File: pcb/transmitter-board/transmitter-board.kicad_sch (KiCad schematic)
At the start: 0 parts

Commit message: Add transmitter-board schematics
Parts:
- added BT1: Battery, Battery:BatteryHolder_Keystone_1042_1x18650, symbol Device:Battery
- added C1: 1n, Capacitor_SMD:C_0805_2012Metric_Pad1.18x1.45mm_HandSolder, symbol Device:C
- added C2: 10n, Capacitor_SMD:C_0805_2012Metric_Pad1.18x1.45mm_HandSolder, symbol Device:C
- added C4, C6: 0.1u, Capacitor_SMD:C_0805_2012Metric_Pad1.18x1.45mm_HandSolder, symbol Device:C
- added C7: 10u, Capacitor_SMD:C_0805_2012Metric_Pad1.18x1.45mm_HandSolder, symbol Device:C
- added D1: R LED, LED_SMD:LED_0805_2012Metric_Pad1.15x1.40mm_HandSolder, symbol Device:LED
- added D2: B LED, LED_SMD:LED_0805_2012Metric_Pad1.15x1.40mm_HandSolder, symbol Device:LED
- added D5: IR LED, LED_THT:LED_D1.8mm_W1.8mm_H2.4mm_Horizontal_O3.81mm_Z8.2mm, symbol Device:LED
- added J1: USB_C_Receptacle_PowerOnly_6P, Connector_USB:USB_C_Receptacle_GCT_USB4125-xx-x-0190_6P_TopMnt_Horizontal, symbol Connector:USB_C_Receptacle_PowerOnly_6P
- added Q1: BC817, Package_TO_SOT_SMD:SOT-23, symbol Transistor_BJT:BC817
- added Q3, Q4: AO3400A, Package_TO_SOT_SMD:SOT-23, symbol Transistor_FET:AO3400A
- added R1, R4, R7, R9: 1k, Resistor_SMD:R_0805_2012Metric_Pad1.20x1.40mm_HandSolder, symbol Device:R
- added R10: 100R, Resistor_SMD:R_0805_2012Metric_Pad1.20x1.40mm_HandSolder, symbol Device:R
- added R11: 18, Resistor_SMD:R_0805_2012Metric_Pad1.20x1.40mm_HandSolder, symbol Device:R
- added R12: 180, Resistor_SMD:R_0805_2012Metric_Pad1.20x1.40mm_HandSolder, symbol Device:R
- added R2: 18.4k, Resistor_SMD:R_0805_2012Metric_Pad1.20x1.40mm_HandSolder, symbol Device:R
- added R3, R6: 5.1k, Resistor_SMD:R_0805_2012Metric_Pad1.20x1.40mm_HandSolder, symbol Device:R
- added R5: 1.2k, Resistor_SMD:R_0805_2012Metric_Pad1.20x1.40mm_HandSolder, symbol Device:R
- added U1: NE555D, Package_SO:SOIC-8_3.9x4.9mm_P1.27mm, symbol Timer:NE555D
- added U3: TP4056-42-ESOP8, Package_SO:SOIC-8-1EP_3.9x4.9mm_P1.27mm_EP2.41x3.3mm_ThermalVias, symbol Battery_Management:TP4056-42-ESOP8
- added U4: DW01A, Package_TO_SOT_SMD:SOT-23-6, symbol Battery_Management:DW01A
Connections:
- new net: R7.1, U3.7 (~{CHRG})
- new net: D1.1 (K), R7.2
- new net: R9.1, U4.2 (CS)
- new net: Q4.1 (G), U4.1 (OD)
- new net: Q3.1 (G), U4.3 (OC)
- new net: C6.1, R10.2, U4.5 (VCC)
- new net: Q3.3 (D), Q4.3 (D)
- new net: R5.1, U3.2 (PROG)
- new net: R4.1, U3.6 (~{STDBY})
- new net: D2.1 (K), R4.2
- new net: C1.1, R2.2, U1.2 (TR), U1.6 (THR)
- new net: R1.2, R2.1, U1.7 (DIS)
- new net: C2.1, U1.5 (CV)
- new net: J1.B5 (CC2), R3.1
- new net: J1.A5 (CC1), R6.1
- new net: D5.1 (K), Q1.3 (C)
- new net: D5.2 (A), R11.2
- new net: Q1.1 (B), R12.2
- new net +3V8: BT1.1 (+), C7.1, R1.1, R10.1, R11.1, U1.4 (R), U1.8 (VCC), U3.5 (BAT)
- new net 555OUT: R12.1, U1.3 (Q)
- new net GND: BT1.2 (-), C1.2, C2.2, C4.2, C6.2, C7.2, J1.A12 (GND), J1.B12 (GND), Q1.2 (E), Q3.2 (S), Q4.2 (S), R3.2, R5.2, R6.2, R9.2, U1.1 (GND), U3.1 (TEMP), U3.3 (GND), U4.6 (GND)
- new net IN+: C4.1, D1.2 (A), D2.2 (A), J1.A9 (VBUS), J1.B9 (VBUS), U3.4 (V_{CC}), U3.8 (CE)
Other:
- note added: "Battery Charger"
- note added: "Battery Protection"
- note added: "IR Diode Circuit"
- note added: "Square Wave Generator (38.175 kHz, 51.32% duty cycle)"
- note added: "USB Connector"

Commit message: Change package to 0603
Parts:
- C1, C2, C4, C6, C7: footprint Capacitor_SMD:C_0805_2012Metric_Pad1.18x1.45mm_HandSolder -> Capacitor_SMD:C_0603_1608Metric_Pad1.08x0.95mm_HandSolder
- D1, D2: footprint LED_SMD:LED_0805_2012Metric_Pad1.15x1.40mm_HandSolder -> LED_SMD:LED_0603_1608Metric_Pad1.05x0.95mm_HandSolder
- R1, R10, R11, R12, R2, R3, R4, R5, R6, R7, R9: footprint Resistor_SMD:R_0805_2012Metric_Pad1.20x1.40mm_HandSolder -> Resistor_SMD:R_0603_1608Metric_Pad0.98x0.95mm_HandSolder
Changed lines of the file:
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@@
 			)
 		)
-		(property "Footprint" "Capacitor_SMD:C_0805_2012Metric_Pad1.18x1.45mm_HandSolder"
+		(property "Footprint" "Capacitor_SMD:C_0603_1608Metric_Pad1.08x0.95mm_HandSolder"
 			(at 65.7352 129.54 0)
 			(effects
@@
 			)
 		)
-		(property "Footprint" "Resistor_SMD:R_0805_2012Metric_Pad1.20x1.40mm_HandSolder"
+		(property "Footprint" "Resistor_SMD:R_0603_1608Metric_Pad0.98x0.95mm_HandSolder"
 			(at 57.912 106.68 90)
 			(effects
@@
 			)
 		)
-		(property "Footprint" "Resistor_SMD:R_0805_2012Metric_Pad1.20x1.40mm_HandSolder"
+		(property "Footprint" "Resistor_SMD:R_0603_1608Metric_Pad0.98x0.95mm_HandSolder"
 			(at 79.502 102.87 90)
 			(effects
@@
 			)
 		)
-		(property "Footprint" "Capacitor_SMD:C_0805_2012Metric_Pad1.18x1.45mm_HandSolder"
+		(property "Footprint" "Capacitor_SMD:C_0603_1608Metric_Pad1.08x0.95mm_HandSolder"
 			(at 122.2248 99.06 0)
 			(effects
@@
 			)
 		)
-		(property "Footprint" "Resistor_SMD:R_0805_2012Metric_Pad1.20x1.40mm_HandSolder"
+		(property "Footprint" "Resistor_SMD:R_0603_1608Metric_Pad0.98x0.95mm_HandSolder"
 			(at 27.178 102.87 90)
 			(effects
@@
 			)
 		)
-		(property "Footprint" "Resistor_SMD:R_0805_2012Metric_Pad1.20x1.40mm_HandSolder"
+		(property "Footprint" "Resistor_SMD:R_0603_1608Metric_Pad0.98x0.95mm_HandSolder"
 			(at 61.722 106.68 90)
 			(effects
@@
 			)
 		)
-		(property "Footprint" "Capacitor_SMD:C_0805_2012Metric_Pad1.18x1.45mm_HandSolder"
+		(property "Footprint" "Capacitor_SMD:C_0603_1608Metric_Pad1.08x0.95mm_HandSolder"
 			(at 69.5452 60.96 0)
 			(effects
@@
 			)
 		)
-		(property "Footprint" "Resistor_SMD:R_0805_2012Metric_Pad1.20x1.40mm_HandSolder"
+		(property "Footprint" "Resistor_SMD:R_0603_1608Metric_Pad0.98x0.95mm_HandSolder"
 			(at 74.422 48.26 90)
 			(effects
@@
 			)
 		)
-		(property "Footprint" "Capacitor_SMD:C_0805_2012Metric_Pad1.18x1.45mm_HandSolder"
+		(property "Footprint" "Capacitor_SMD:C_0603_1608Metric_Pad1.08x0.95mm_HandSolder"
 			(at 36.5252 62.23 0)
 			(effects
@@
 			)
 		)
-		(property "Footprint" "Resistor_SMD:R_0805_2012Metric_Pad1.20x1.40mm_HandSolder"
+		(property "Footprint" "Resistor_SMD:R_0603_1608Metric_Pad0.98x0.95mm_HandSolder"
 			(at 70.612 175.26 90)
 			(effects
@@
 			)
 		)
-		(property "Footprint" "LED_SMD:LED_0805_2012Metric_Pad1.15x1.40mm_HandSolder"
+		(property "Footprint" "LED_SMD:LED_0603_1608Metric_Pad1.05x0.95mm_HandSolder"
 			(at 59.69 115.57 0)
 			(effects
@@
 			)
 		)
-		(property "Footprint" "LED_SMD:LED_0805_2012Metric_Pad1.15x1.40mm_HandSolder"
+		(property "Footprint" "LED_SMD:LED_0603_1608Metric_Pad1.05x0.95mm_HandSolder"
 			(at 63.5 115.57 0)
 			(effects
@@
 			)
 		)
-		(property "Footprint" "Resistor_SMD:R_0805_2012Metric_Pad1.20x1.40mm_HandSolder"
+		(property "Footprint" "Resistor_SMD:R_0603_1608Metric_Pad0.98x0.95mm_HandSolder"
 			(at 118.11 89.408 90)
 			(effects
@@
 			)
 		)
-		(property "Footprint" "Capacitor_SMD:C_0805_2012Metric_Pad1.18x1.45mm_HandSolder"
+		(property "Footprint" "Capacitor_SMD:C_0603_1608Metric_Pad1.08x0.95mm_HandSolder"
 			(at 110.7948 95.25 0)
 			(effects
@@
 			)
 		)
-		(property "Footprint" "Resistor_SMD:R_0805_2012Metric_Pad1.20x1.40mm_HandSolder"
+		(property "Footprint" "Resistor_SMD:R_0603_1608Metric_Pad0.98x0.95mm_HandSolder"
 			(at 129.032 27.94 90)
 			(effects
@@
 			)
 		)
-		(property "Footprint" "Resistor_SMD:R_0805_2012Metric_Pad1.20x1.40mm_HandSolder"
+		(property "Footprint" "Resistor_SMD:R_0603_1608Metric_Pad0.98x0.95mm_HandSolder"
 			(at 79.502 175.26 90)
 			(effects
@@
 			)
 		)
-		(property "Footprint" "Resistor_SMD:R_0805_2012Metric_Pad1.20x1.40mm_HandSolder"
+		(property "Footprint" "Resistor_SMD:R_0603_1608Metric_Pad0.98x0.95mm_HandSolder"
 			(at 74.422 38.1 90)
 			(effects
@@
 			)
 		)
-		(property "Footprint" "Resistor_SMD:R_0805_2012Metric_Pad1.20x1.40mm_HandSolder"
+		(property "Footprint" "Resistor_SMD:R_0603_1608Metric_Pad0.98x0.95mm_HandSolder"
 			(at 115.57 51.308 90)
 			(effects

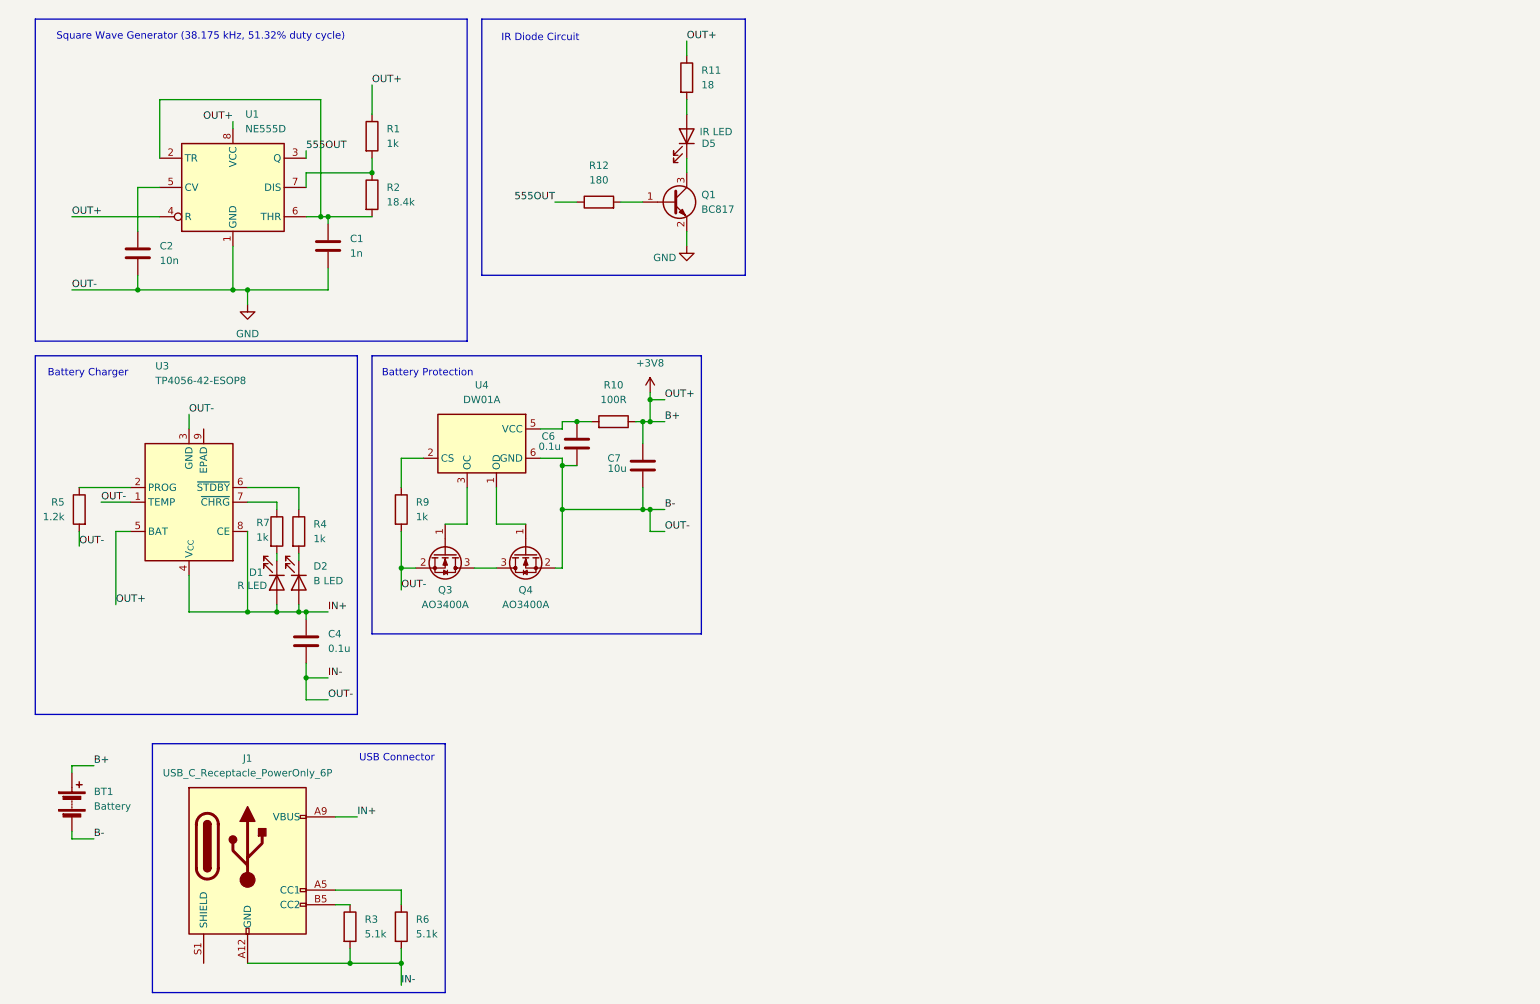
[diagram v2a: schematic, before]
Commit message: Add transmitter-board pcb
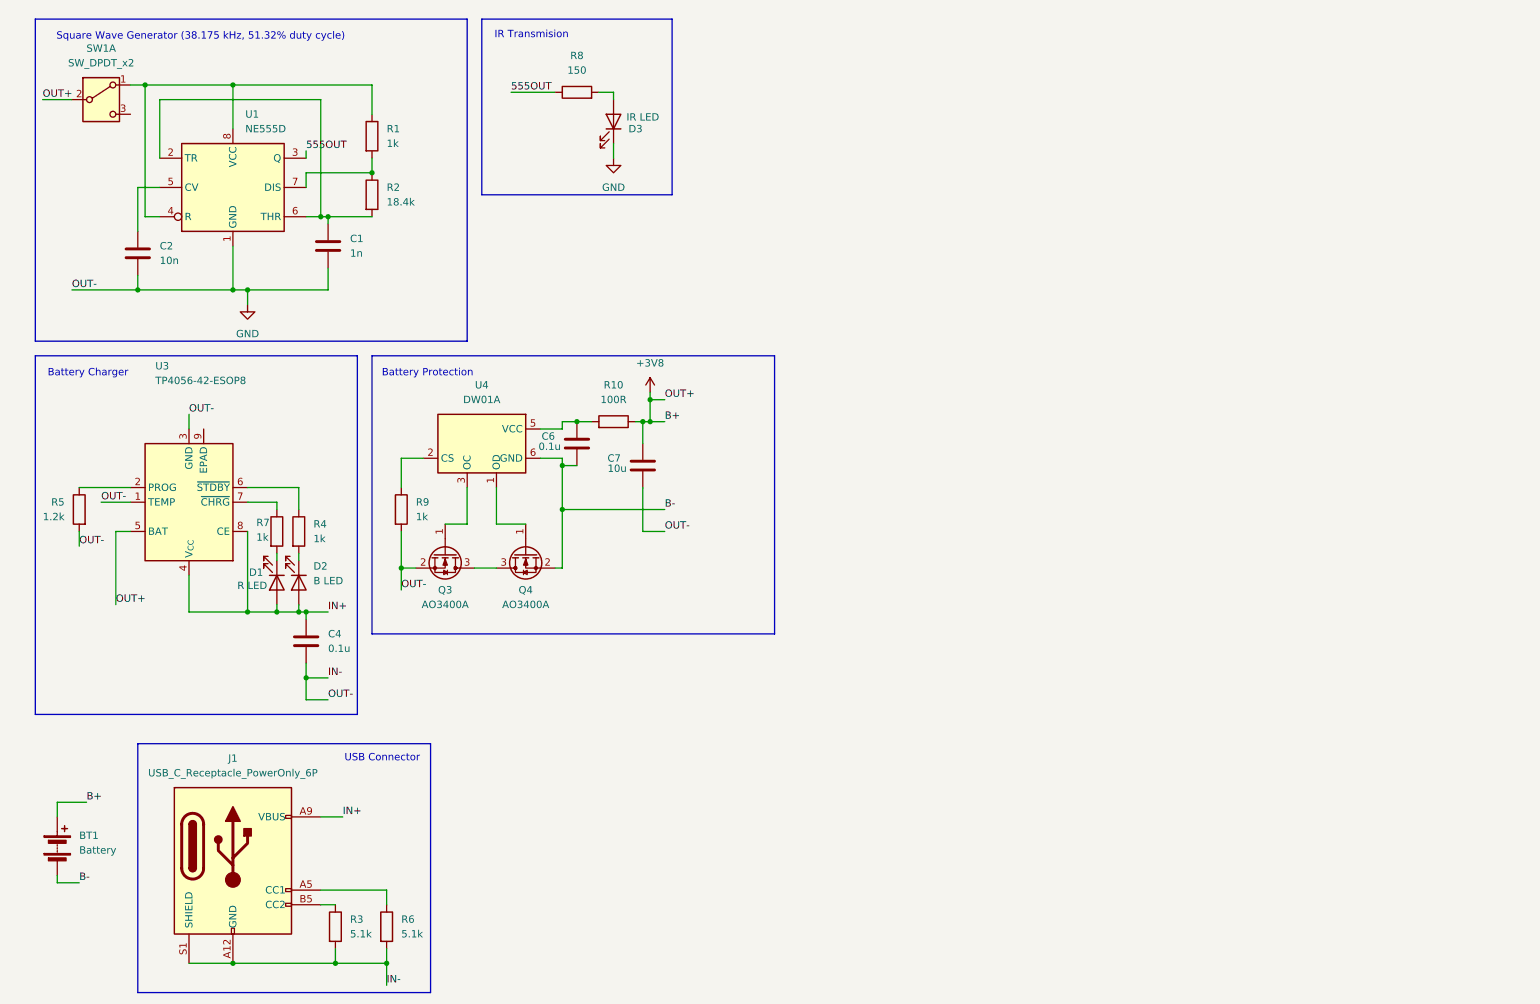
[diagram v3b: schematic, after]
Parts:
- removed D5: IR LED, LED_THT:LED_D1.8mm_W1.8mm_H2.4mm_Horizontal_O3.81mm_Z8.2mm, symbol Device:LED
- removed Q1: BC817, Package_TO_SOT_SMD:SOT-23, symbol Transistor_BJT:BC817
- removed R11: 18, Resistor_SMD:R_0603_1608Metric_Pad0.98x0.95mm_HandSolder, symbol Device:R
- removed R12: 180, Resistor_SMD:R_0603_1608Metric_Pad0.98x0.95mm_HandSolder, symbol Device:R
- added D3: IR LED, LED_THT:LED_THT_Horizontal_SMD_mounted, symbol Device:LED
- added R8: 150, Resistor_SMD:R_0603_1608Metric_Pad0.98x0.95mm_HandSolder, symbol Device:R
- added SW1: SW_DPDT_x2, Button_Switch_SMD:SW_DPDT_CK_JS202011JCQN, symbol Switch:SW_DPDT_x2
- BT1: footprint Battery:BatteryHolder_Keystone_1042_1x18650 -> Connector_PinSocket_2.54mm:PinSocket_1x02_P2.54mm_Vertical_SMD_Pin1Left
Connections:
- net +3V8: now also SW1.2 (B); no longer R1.1, U1.4 (R), U1.8 (VCC)
- net 555OUT: now also R8.1
- net GND: now also J1.S1 (SHIELD), D3.1 (K); no longer BT1.2 (-), C6.2, Q4.2 (S), U4.6 (GND)
- new net: R1.1, SW1.1 (A), U1.4 (R), U1.8 (VCC)
- new net: D3.2 (A), R8.2
- new net B-: BT1.2 (-), C6.2, Q4.2 (S), U4.6 (GND)
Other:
- note added: "IR Transmision"
- note removed: "IR Diode Circuit"
- moved on the sheet: BT1, J1, R3, R6

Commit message: Change hole size under TP4056 and change battery connector to THT.
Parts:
- BT1: footprint Connector_PinSocket_2.54mm:PinSocket_1x02_P2.54mm_Vertical_SMD_Pin1Left -> Connector_PinSocket_2.54mm:PinSocket_1x02_P2.54mm_Vertical
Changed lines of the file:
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@@
 			)
 		)
-		(property "Footprint" "Connector_PinSocket_2.54mm:PinSocket_1x02_P2.54mm_Vertical_SMD_Pin1Left"
+		(property "Footprint" "Connector_PinSocket_2.54mm:PinSocket_1x02_P2.54mm_Vertical"
 			(at 21.59 159.766 90)
 			(effects

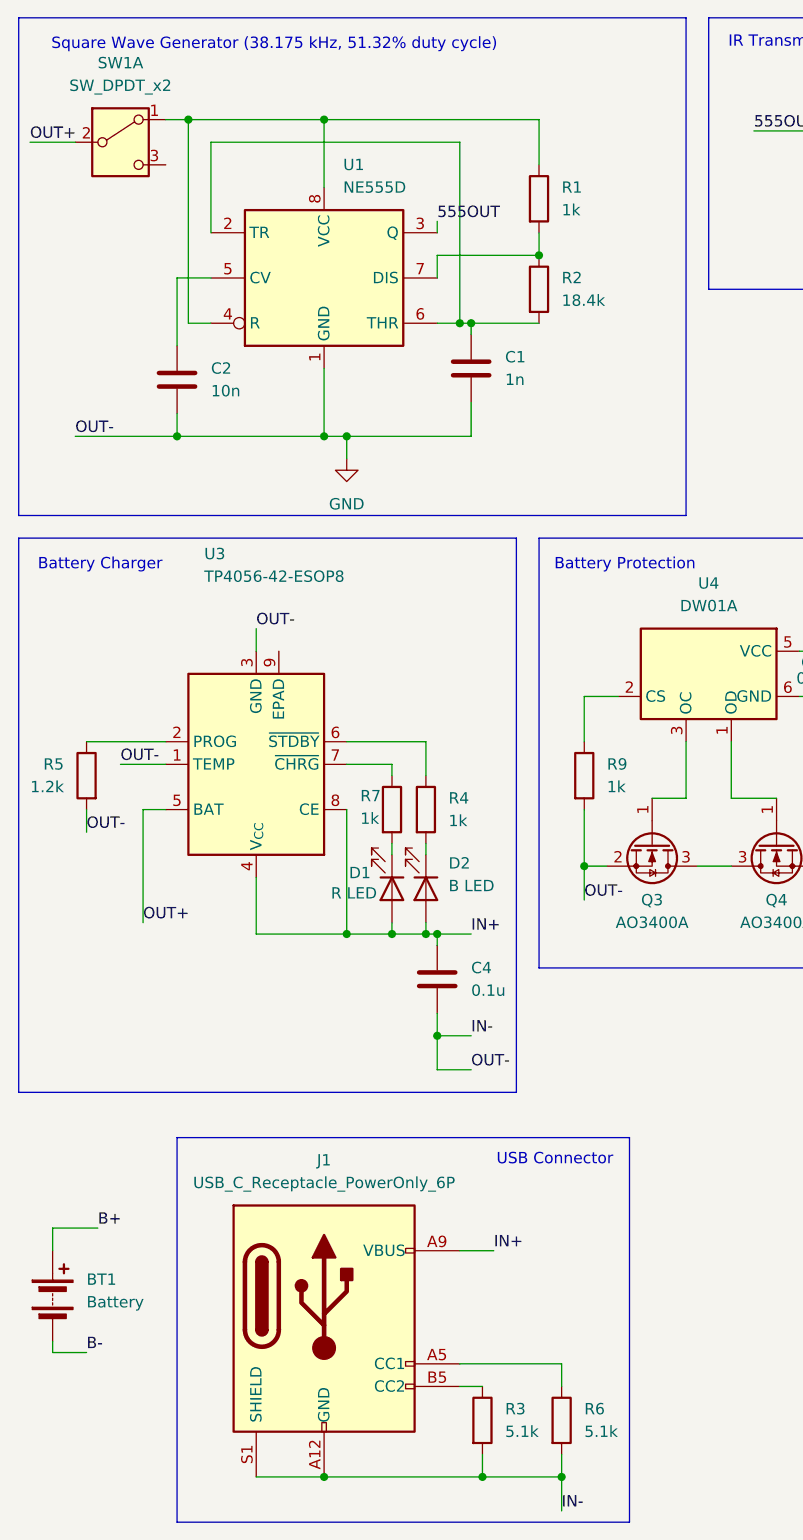
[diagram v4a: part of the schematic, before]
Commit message: Change USB and battery connector
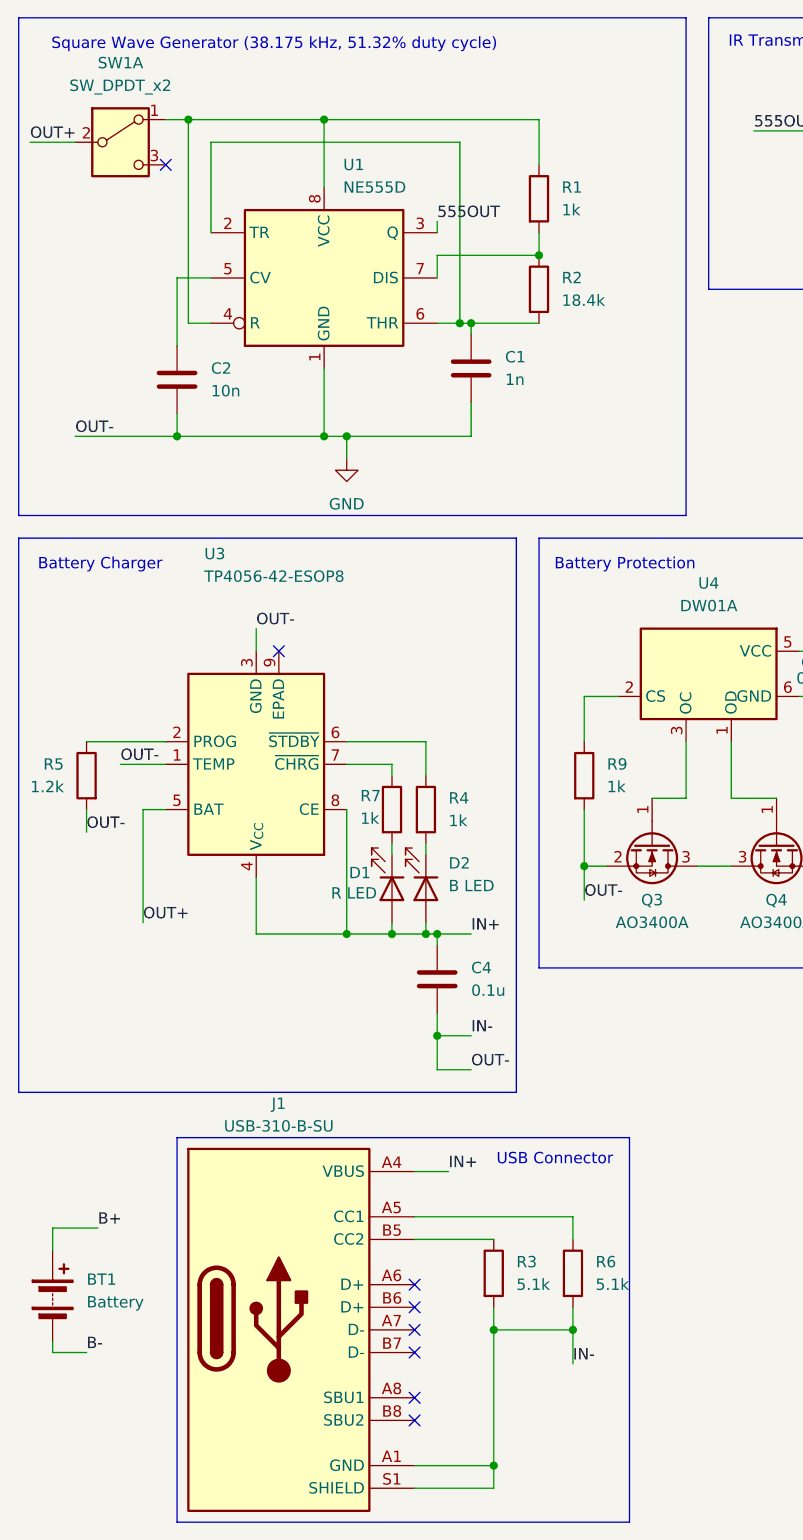
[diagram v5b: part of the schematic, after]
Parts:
- removed J1: USB_C_Receptacle_PowerOnly_6P, Connector_USB:USB_C_Receptacle_GCT_USB4125-xx-x-0190_6P_TopMnt_Horizontal, symbol Connector:USB_C_Receptacle_PowerOnly_6P
- added J1: USB-C_USB-310F-B-SU, DW-footprints:USB-C-Receptacle_USB-310-B-SU, symbol DW-connectors:USB-C_USB-310-B-SU
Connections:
- net GND: now also J1.A1 (GND), J1.A12 (GND), J1.B1 (GND), J1.B12 (GND), J1.S1 (SHIELD)
- net IN+: now also J1.A4 (VBUS), J1.A9 (VBUS), J1.B4 (VBUS), J1.B9 (VBUS)
- net at R3.1: now also J1.B5 (CC2)
- net at R6.1: now also J1.A5 (CC1)
- no-connect marks 0 -> 8
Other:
- moved on the sheet: R3, R6

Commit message: Change R5 value
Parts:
- R5: value 1.2k -> 10k
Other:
- note added: "R_{PROG} = 1100/I_{BAT}"
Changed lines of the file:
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@@
+		)
+	)
+	(text "R_{PROG} = 1100/I_{BAT}"
+		(exclude_from_sim no)
+		(at 21.59 99.568 0)
+		(effects
+			(font
+				(size 0.5 0.5)
+			)
 		)
 	)
@@
 			)
 		)
-		(property "Value" "1.2k"
+		(property "Value" "10k"
 			(at 22.86 104.1399 0)
 			(effects
